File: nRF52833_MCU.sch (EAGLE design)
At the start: 20 parts, among them IC1 SKY13415-485LF, IC2 BQ25570RGRR, J100 DEBUG_CONNECTOR, X1 32MHz, X2 32.768kHz

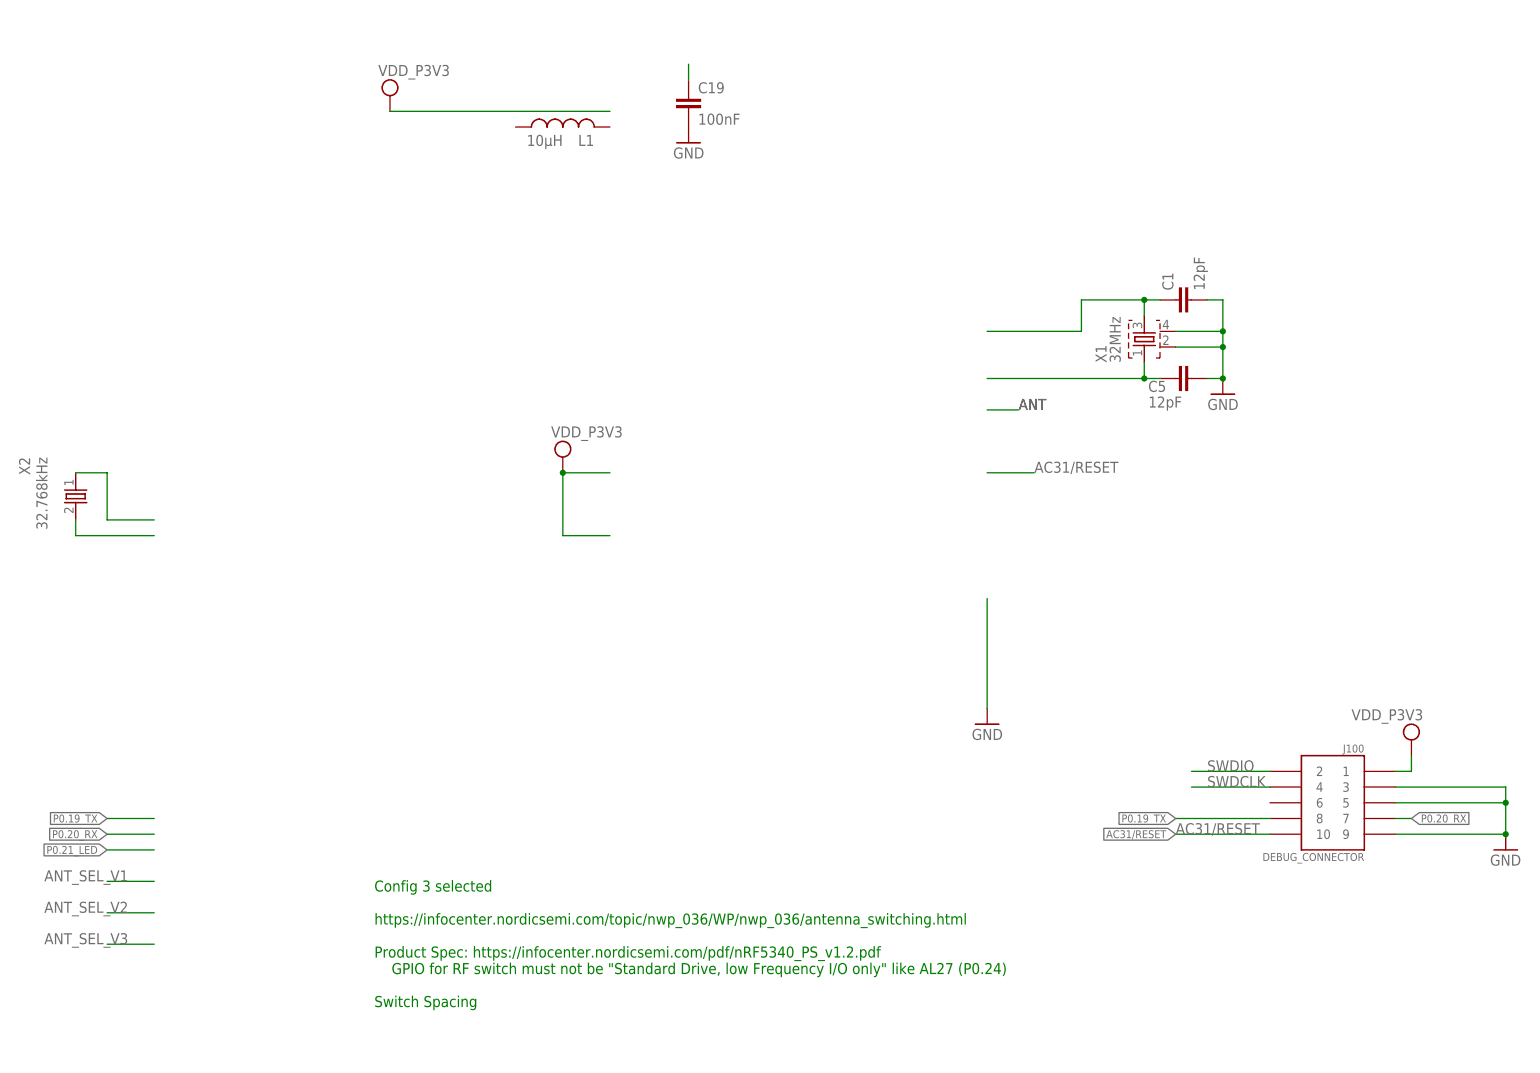
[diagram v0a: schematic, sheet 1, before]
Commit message: Add gpios for nrf52833
Signed-off-by: Florian Depraz <florian.depraz@outlook.com>
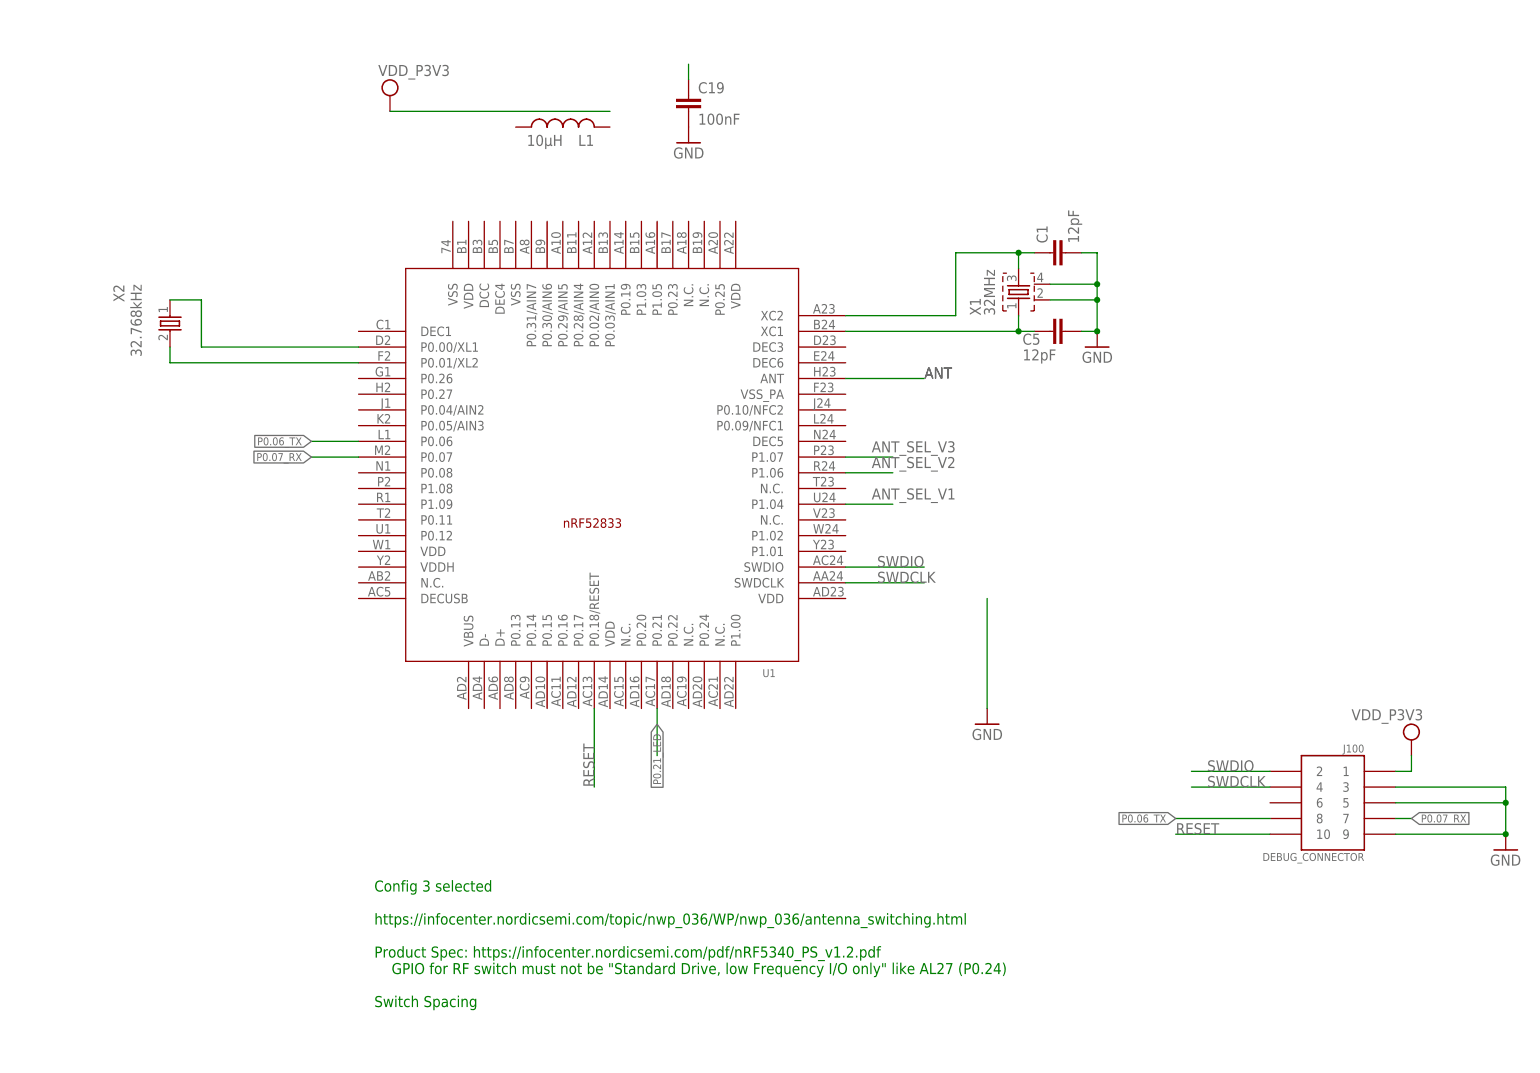
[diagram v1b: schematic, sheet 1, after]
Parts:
- added U1: nRF52833-QIAA, nrf52833_qiaa:NRF52833_QIAANRF52833_QIAA_AQFN50P700X700X85_HS-74N
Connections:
- removed net AC31/RESET: J100.10
- removed net P0.19_TX: J100.8
- removed net P0.20_RX: J100.7
- new net P0.06_TX: J100.8, U1.P0.06
- new net P0.07_RX: J100.7, U1.P0.07
- new net RESET: J100.10, U1.P0.18/RESET
- net ANT: now also U1.ANT
- net ANT_SEL_V1: now also U1.P1.04
- net ANT_SEL_V2: now also U1.P1.06
- net ANT_SEL_V3: now also U1.P1.07
- net N$3: now also U1.XC2
- net N$37: now also U1.XC1
- net N$38: now also U1.P0.00/XL1
- net N$39: now also U1.P0.01/XL2
- net P0.21_LED: now also U1.P0.21
- net SWDCLK: now also U1.SWDCLK
- net SWDIO: now also U1.SWDIO
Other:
- moved on the sheet: C1, C5, X1, X2

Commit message: Add capa for option 3 nrf52833
Signed-off-by: Florian Depraz <florian.depraz@outlook.com>
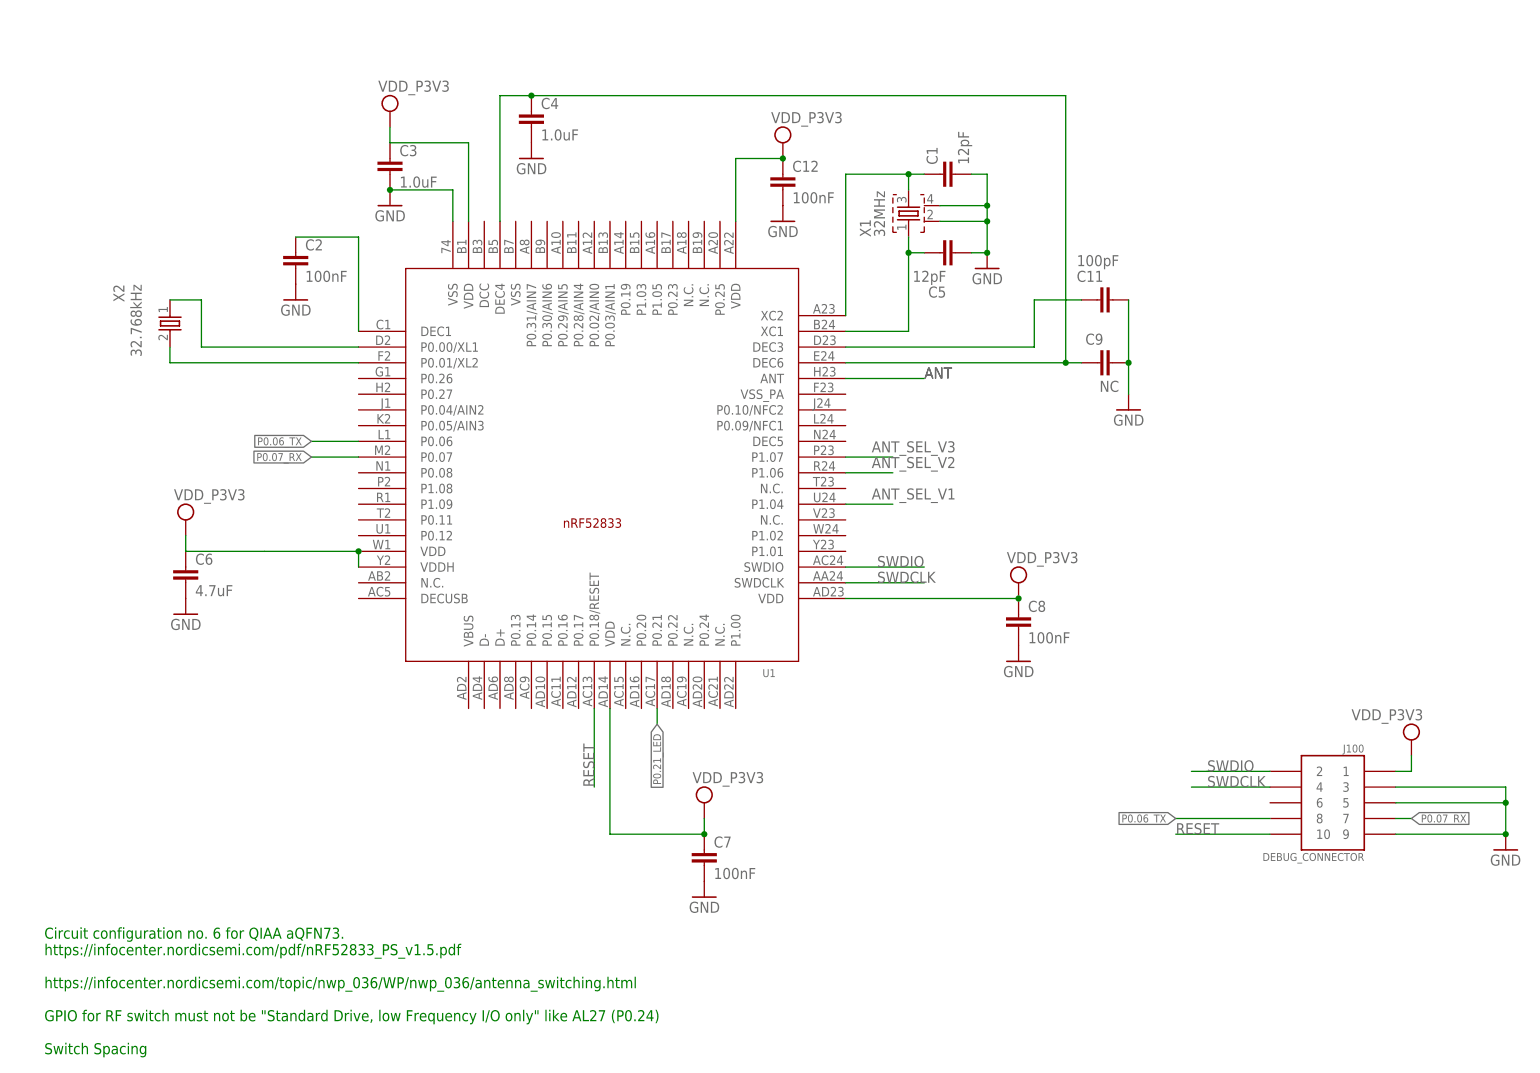
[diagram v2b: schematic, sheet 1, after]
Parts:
- removed C19: 100nF, Nordic_misc:CAPACITOR_0402_N
- removed L1: 10µH, Nordic_misc:INDUCTOR_0603_N
- added C11: 100pF, Nordic_misc:CAPACITOR_0402_N
- added C12, C2, C7, C8: 100nF, Nordic_misc:CAPACITOR_0402_N
- added C3, C4: 1.0uF, Nordic_misc:CAPACITOR_0402_N
- added C6: 4.7uF, Nordic_misc:CAPACITOR_0402_N
- added C9: NC, Nordic_misc:CAPACITOR_0402_N
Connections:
- removed net N$36: C19.1
- new net N$18: C12.1, C3.1, C6.1, C7.1, C8.1, U1.VDD@1, U1.VDD@2, U1.VDD@3, U1.VDD@4, U1.VDD@5, U1.VDDH
- new net N$19: C4.1, C9.1, U1.DEC4, U1.DEC6
- new net N$2: C2.1, U1.DEC1
- new net N$21: C11.1, U1.DEC3
- net GND: now also C11.2, C12.2, C2.2, C3.2, C4.2, C6.2, C7.2, C8.2, C9.2, U1.VSS@1; no longer C19.2
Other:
- note added: "Circuit configuration no. 6 for QIAA aQFN73. https://infocenter.nordicsemi.com/pdf/nRF52833_PS_v1.5.pdf https://infocenter.nordicsemi.com/topic/nwp_036/WP/nwp_036/antenna_switching.html GPIO for RF switch must not be "Standard Drive, low Frequency I/O only" like AL27 (P0.24) Switch Spacing"
- note removed: "Config 3 selected https://infocenter.nordicsemi.com/topic/nwp_036/WP/nwp_036/antenna_switching.html Product Spec: https://infocenter.nordicsemi.com/pdf/nRF5340_PS_v1.2.pdf GPIO for RF switch must not be "Standard Drive, low Frequency I/O only" like AL27 (P0.24) Switch Spacing"
- moved on the sheet: C1, C5, D1, IC1, R5, X1

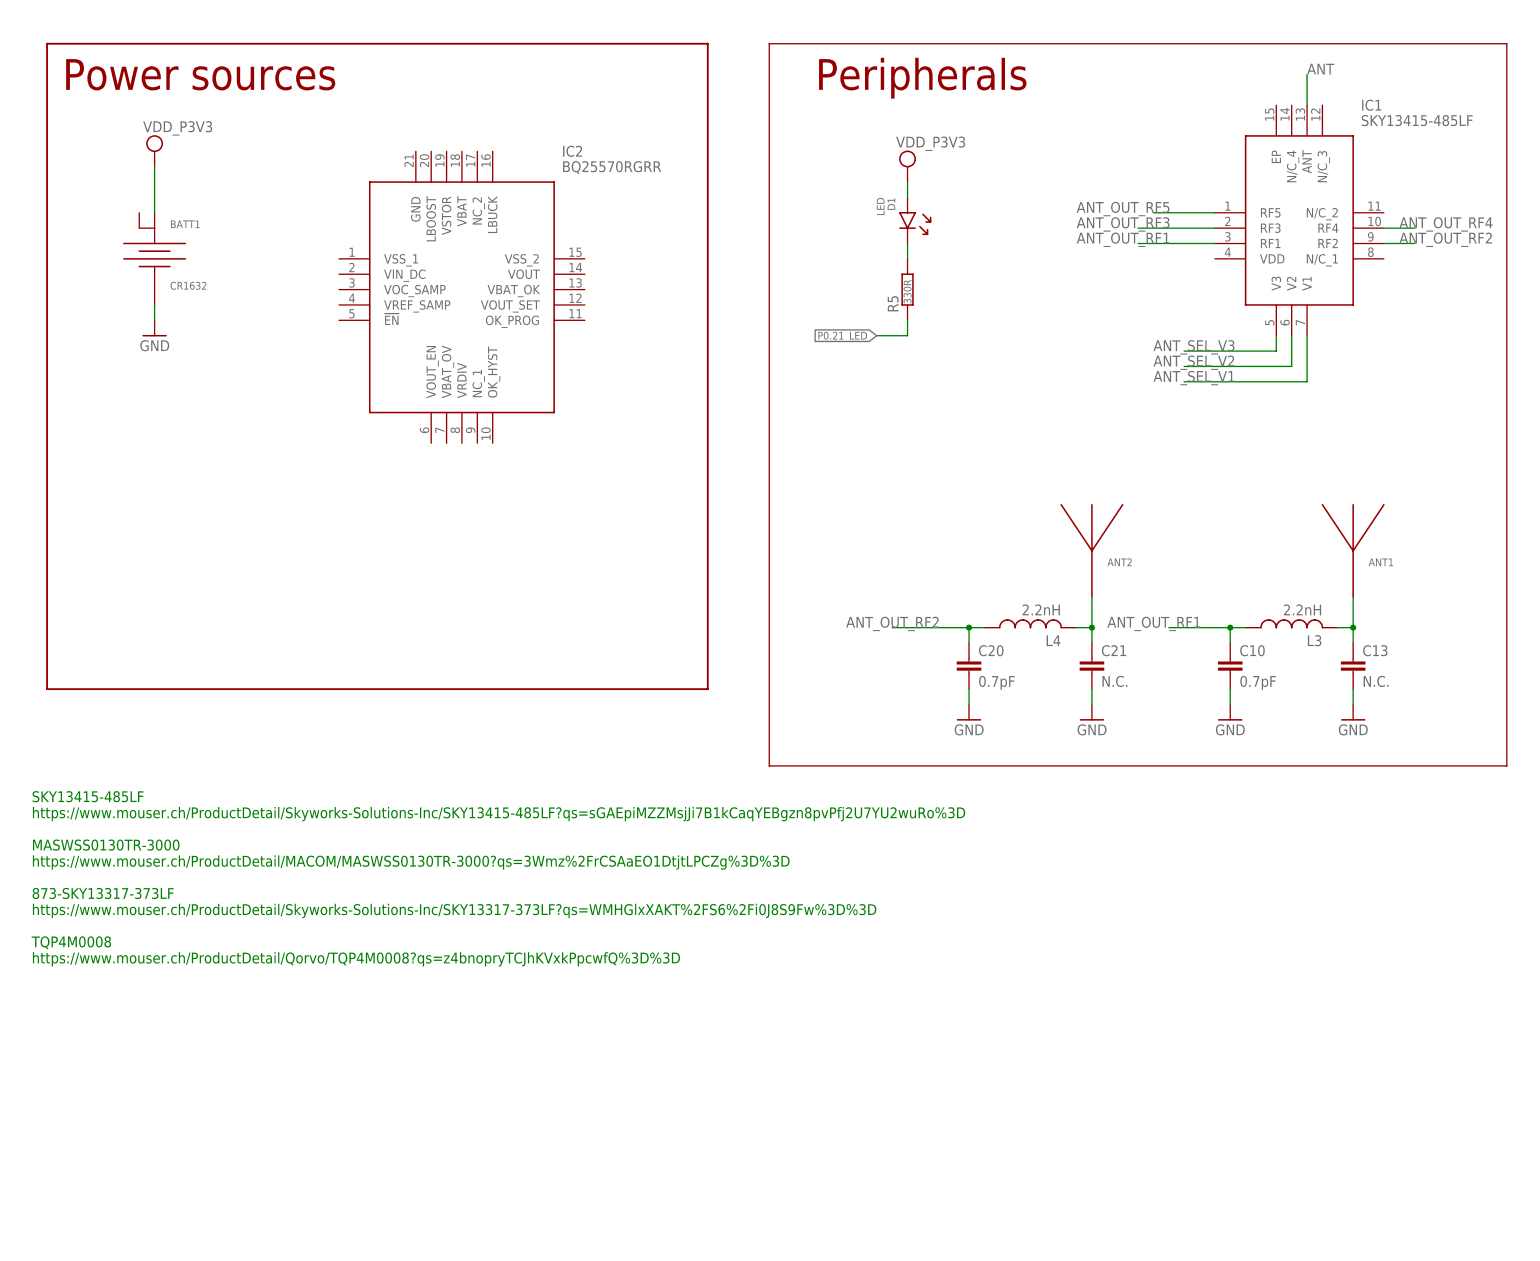
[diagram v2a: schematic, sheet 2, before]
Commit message: Redefine schematic to add energy harvest
Signed-off-by: Florian Depraz <florian.depraz@outlook.com>
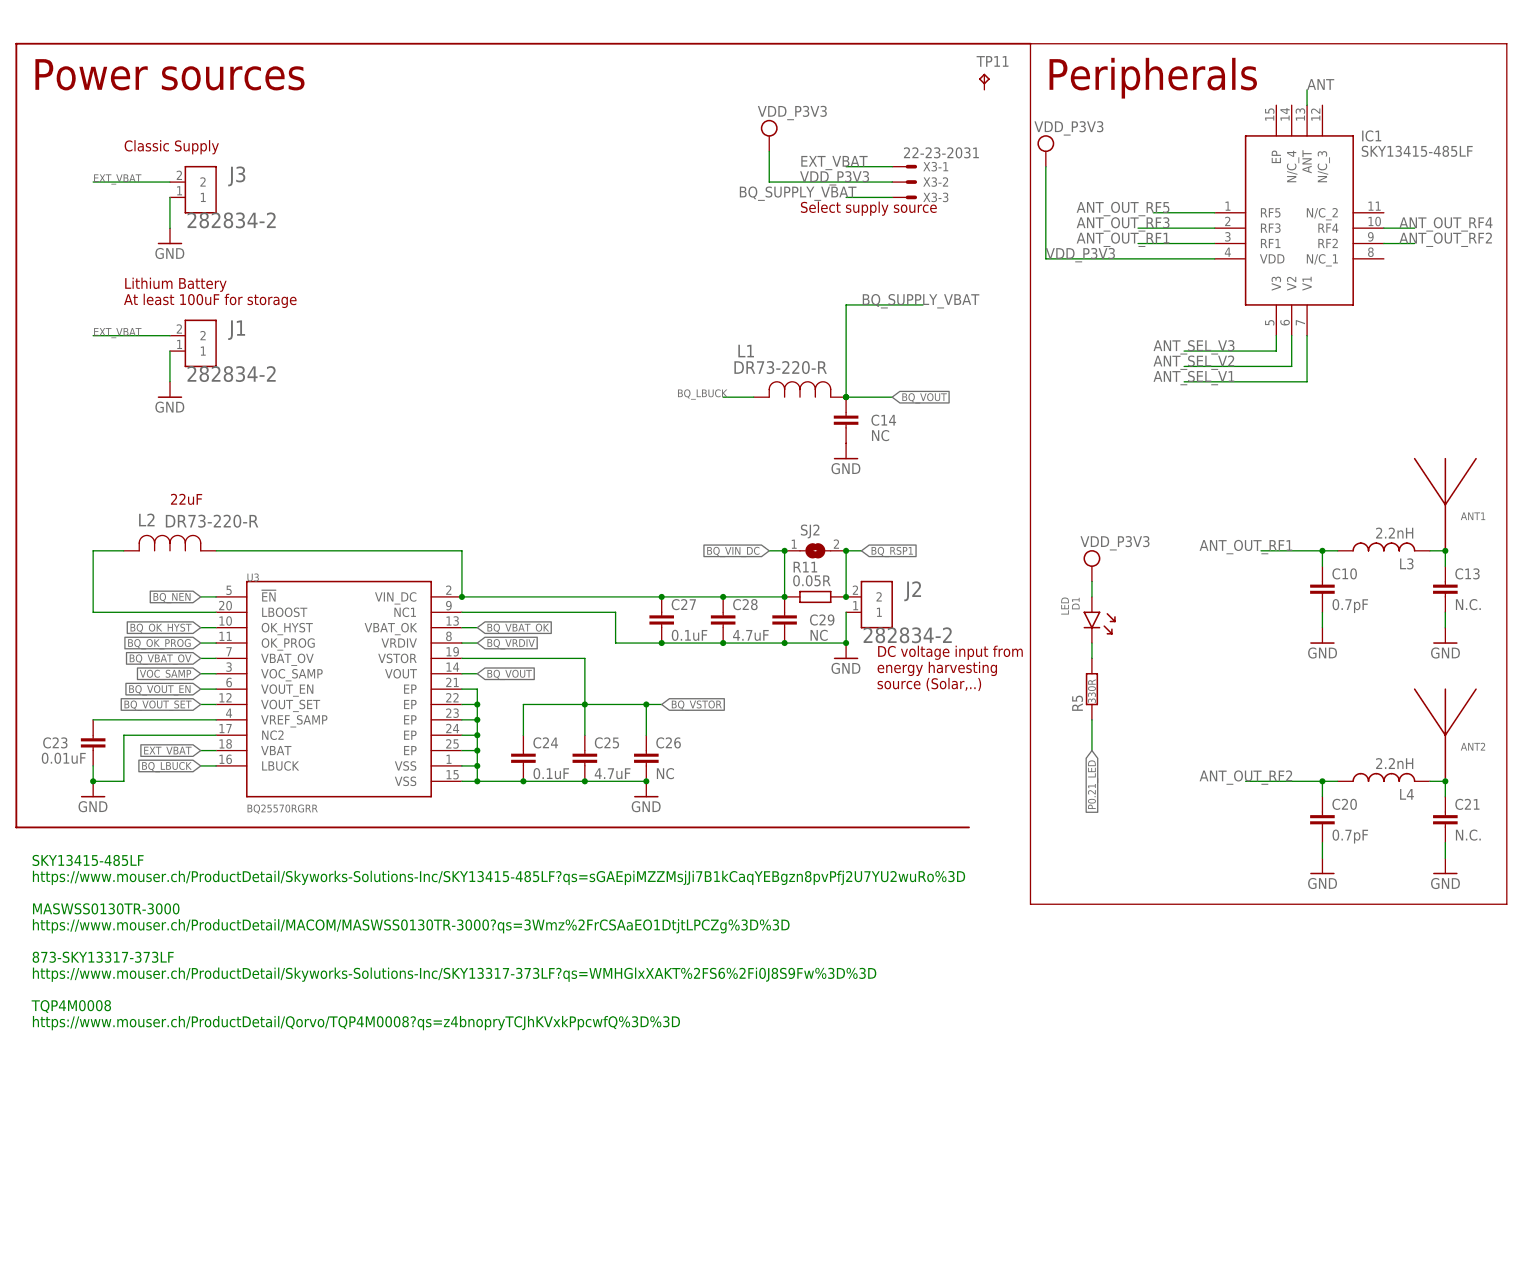
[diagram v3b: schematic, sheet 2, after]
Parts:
- removed BATT1: CR1632, Nordic_misc:CR1632
- removed IC2: BQ25570RGRR, SamacSys_Parts:BQ25570RGRR
- added C14, C26, C29: NC, Nordic_misc:CAPACITOR_0402_N
- added C23: 0.01uF, Nordic_misc:CAPACITOR_0402_N
- added C24, C27: 0.1uF, Nordic_misc:CAPACITOR_0402_N
- added C25, C28: 4.7uF, Nordic_misc:CAPACITOR_0402_N
- added J1, J2, J3: 282834-2, 282834-2:282834-2
- added L1, L2: DR73-220-R, DR73-220-R:DR73-220-R
- added R11: 0.05R, Y14870RXX000B9R:Y14870RXX000B9R
- added SJ2: (no value), jumper:SJ
- added TP11: TPPAD1-13, testpad:TPPAD1-13
- added U3: BQ25570RGRR, BQ25570RGRR:BQ25570RGRR
- added X3: 22-23-2031, con-molex:22-23-2031
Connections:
- net N$18 renamed VDD
- net N$19 renamed DEC6
- net N$2 renamed DEC1
- net N$21 renamed DEC3
- net N$3 renamed XC2
- net N$37 renamed XC1
- net N$38 renamed XL1
- net N$39 renamed XL2
- new net BQ_LBUCK: L1.2, U3.LBUCK
- new net BQ_NEN: U3.!EN
- new net BQ_OK_HYST: U3.OK_HYST
- new net BQ_OK_PROG: U3.OK_PROG
- new net BQ_RSP1: J2.2, R11.2, SJ2.2
- new net BQ_SUPPLY_VBAT: C14.1, L1.1, X3-3.S
- new net BQ_VBAT_OK: U3.VBAT_OK
- new net BQ_VBAT_OV: U3.VBAT_OV
- new net BQ_VIN_DC: C27.1, C28.1, C29.1, L2.1, R11.1, SJ2.1, U3.VIN_DC
- new net BQ_VOUT: U3.VOUT
- new net BQ_VOUT_EN: U3.VOUT_EN
- new net BQ_VOUT_SET: U3.VOUT_SET
- new net BQ_VRDIV: U3.VRDIV
- new net BQ_VSTOR: C24.1, C25.1, C26.1, U3.VSTOR
- new net EXT_VBAT: J1.2, J3.2, U3.VBAT, X3-1.S
- new net LBOOST: L2.2, U3.LBOOST
- new net VOC_SAMP: U3.VOC_SAMP
- new net VREF_SAMP: C23.1, U3.VREF_SAMP
- new net VSS: C3.2, U1.VSS@1
- net GND: now also C14.2, C23.2, C24.2, C25.2, C26.2, C27.2, C28.2, C29.2, J1.1, J2.1, J3.1, U3.EP@1, U3.EP@2, U3.EP@3, U3.EP@4, U3.EP@5, U3.NC1, U3.NC2, U3.VSS@1, U3.VSS@2; no longer BATT1.-, C3.2, U1.VSS@1
- net VDD_P3V3: now also IC1.VDD, X3-2.S; no longer BATT1.+
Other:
- note added: "22uF"
- note added: "Classic Supply"
- note added: "DC voltage input from energy harvesting source (Solar,..)"
- note added: "Lithium Battery At least 100uF for storage"
- note added: "Select supply source"
- moved on the sheet: ANT1, ANT2, C1, C10, C11, C12, C13, C2, C20, C21, C3, C4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
